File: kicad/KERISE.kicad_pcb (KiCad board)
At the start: 2 copper layers, 42 x 47.5 mm, 116 parts, among them J1 USB_OTG, P1 ANT, P10 Partition, P11 PR_Host, P12 PR_Slave, P13 Partition, P14 Partition, P15 Partition, P16 Partition, P17 COM, P18 Fan, P19 ENC_Host, P2 Motor_L, P20 ENC_Slave, P21 ToF_Host, P22 ToF_Slave, P23 COM, P24 ENC_Host, P25 ENC_Slave, P3 Motor_R, P4 Battery, P5 PR_Host, P6 PR_Slave, P7 Partition, P8 Partition, P9 Partition, Q1 IRFML8244, Q2 IRFML8244, Q3 IRFML8244, Q4 IRFML8244, SW1 SW_Push, SW2 SW_Push, U1 FLASH, U10 MCP73831, U11 FT234XD, U12 AS5048A, U13 ICM-20602, U2 ESP32, U3 XTAL, U4 DRV8835, U5 LXDC2URxx, U6 AD8601, U7 AD8601, U8 AS5048A, U9 VL53L0X

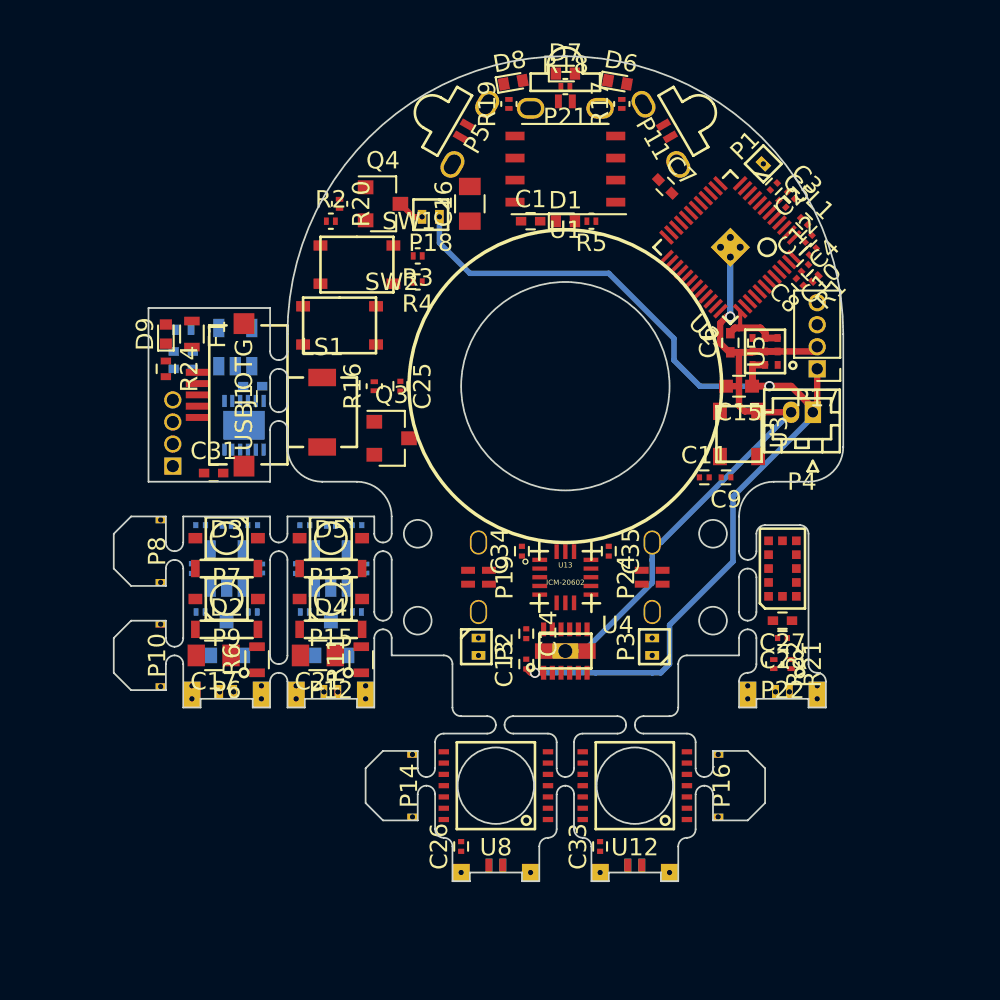
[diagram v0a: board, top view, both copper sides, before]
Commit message: 部品の配置と電源ラインの引き方を変更．
センサ部分にノイズがはいらないように考慮
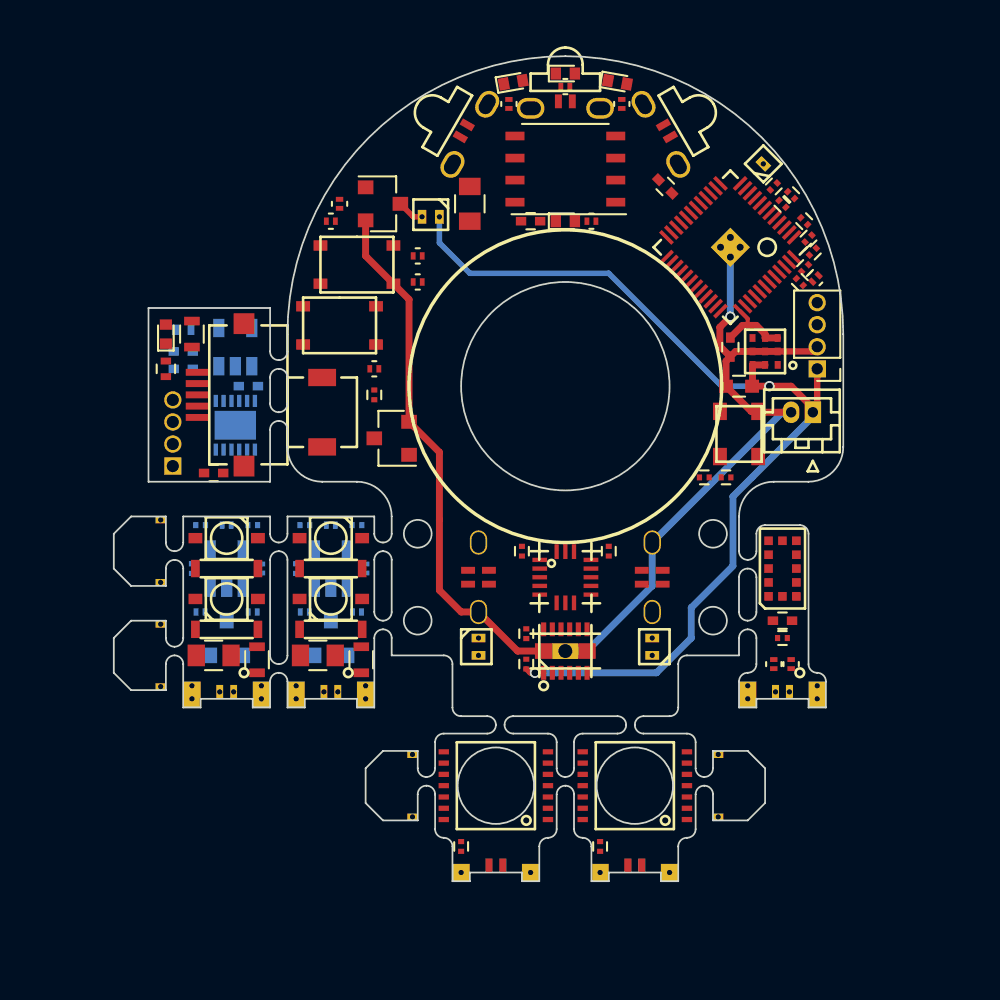
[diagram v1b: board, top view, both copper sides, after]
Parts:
- moved C25 1.58 mm to (137.5, 102.5)
- moved R16 1.00 mm to (137.5, 101.0), turned to 0 degrees
- moved U11 0.50 mm to (129.5, 104.2)
- moved C29 0.25 mm to (130.2, 102.0)
- moved C6 0.25 mm to (158.0, 99.8)
- turned C32 to 0 degrees
- turned Q3 to 180 degrees
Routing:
- net GND: track 38.3 -> 69.7 mm
- net +BATT: track 61.4 -> 59.8 mm
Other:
- net class LED: trace_width 0.3 -> 0.32; via_dia 0.36 -> 0.4; via_drill 0.3 -> 0.36

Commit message: 自動配線成功
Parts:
- C32: moved to F.Cu
- U11: footprint Housings_DFN_QFN:DFN-12-1EP_3x3mm_Pitch0.45mm -> mouse:DFN-12-1EP_3x3mm_Pitch0.45mm
- moved C32 4.60 mm to (126.4, 105.6), turned to 90 degrees
- moved C26 2.50 mm to (142.5, 131.0)
- moved C33 2.50 mm to (150.5, 131.0)
- moved P14 2.50 mm to (140.0, 127.5)
- moved P16 2.50 mm to (157.0, 127.5)
- moved P20 2.50 mm to (144.5, 132.5)
- moved P25 2.50 mm to (152.5, 132.5)
- moved U12 2.50 mm to (152.5, 127.5)
- moved U8 2.50 mm to (144.5, 127.5)
- moved R18 1.25 mm to (147.2, 84.8), turned to 90 degrees
- moved C29 0.79 mm to (129.5, 102.2)
- moved C30 0.71 mm to (126.0, 99.5)
- moved D9 0.71 mm to (125.0, 99.5)
- moved R24 0.71 mm to (125.0, 101.5), turned to 0 degrees
- moved U11 0.62 mm to (128.9, 104.4)
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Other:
- board size 42 x 47.5 mm -> 43 x 50 mm

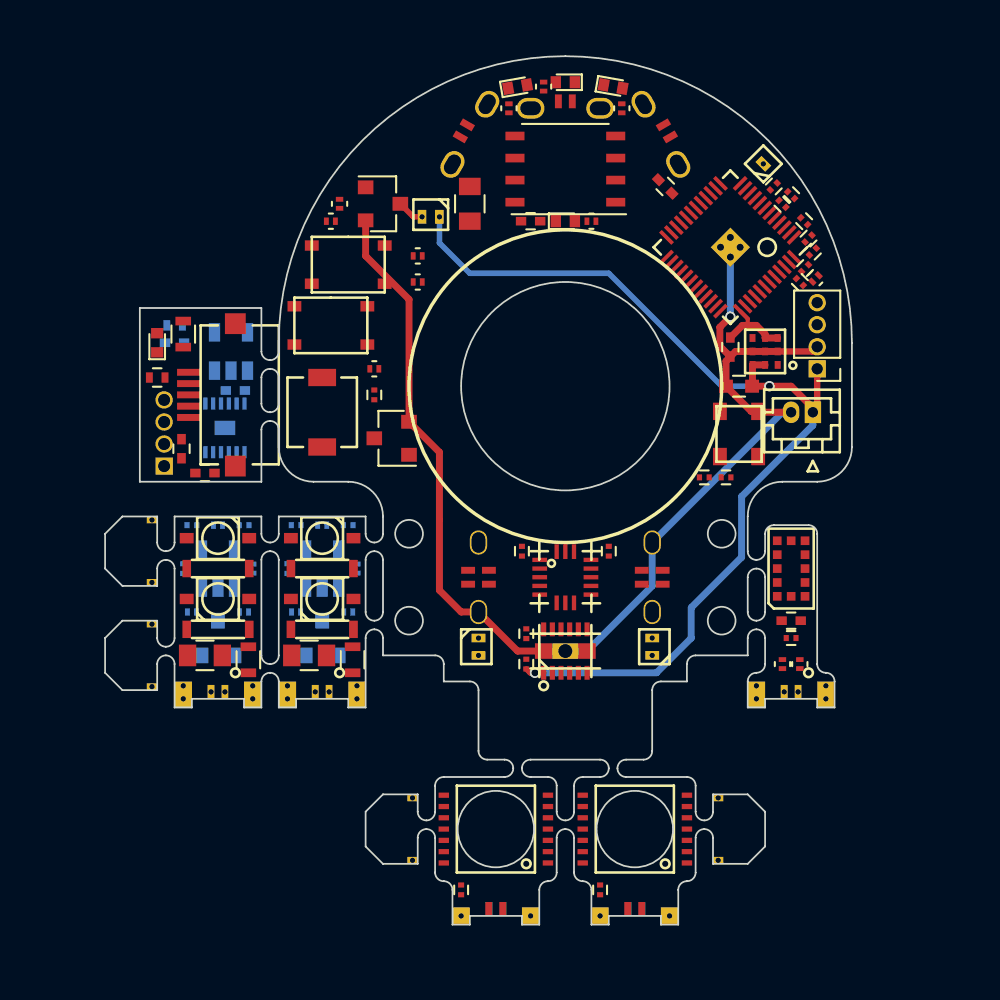
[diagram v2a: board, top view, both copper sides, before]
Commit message: 配線を0.15mmにして自動配線成功
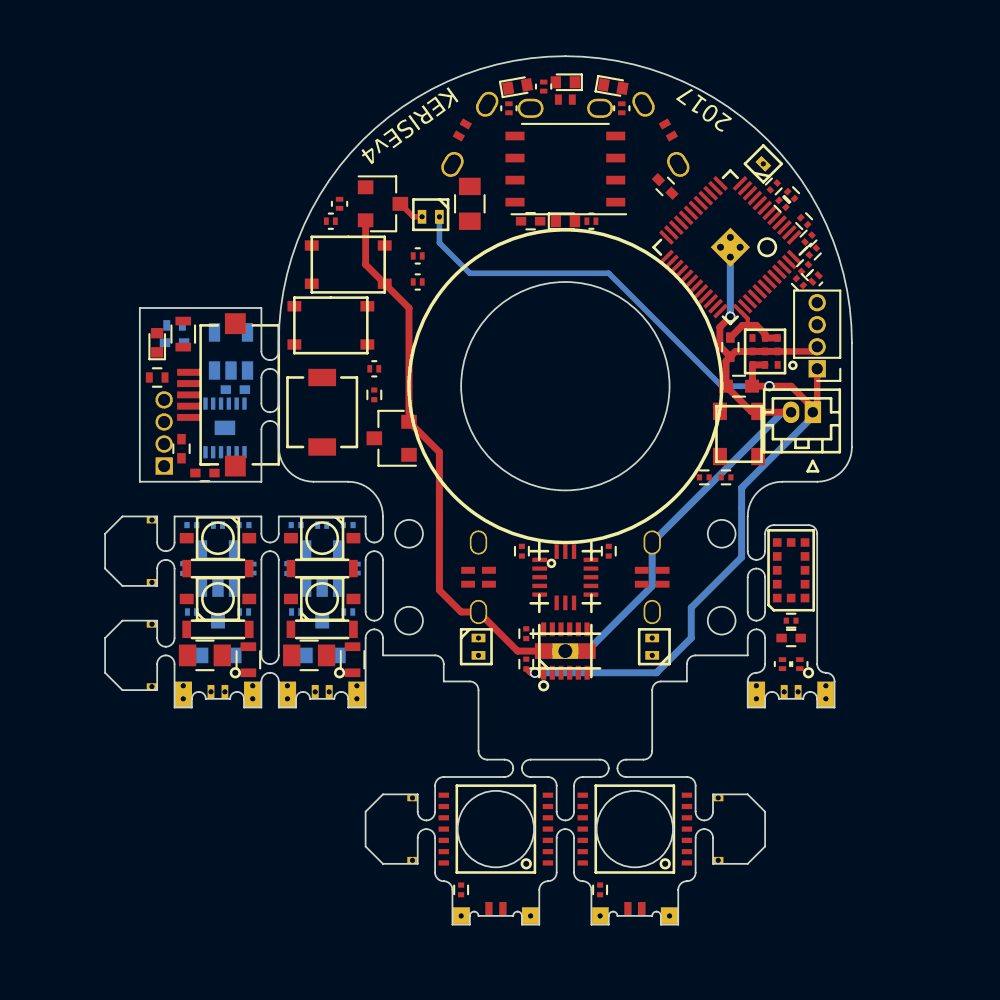
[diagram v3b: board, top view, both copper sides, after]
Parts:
- moved C27 1.00 mm to (161.5, 116.5)
- moved C28 1.00 mm to (161.5, 115.5)
- moved U9 0.10 mm to (161.5, 112.6)
- turned C16 to 270 degrees
- turned C18 to 0 degrees
- turned C22 to 0 degrees
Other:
- outline, holes or cut-outs redrawn
- net class 3.3V: clearance 0.154 -> 0.15; trace_width 0.2 -> 0.16; via_dia 0.34 -> 0.36
- net class BATT: clearance 0.154 -> 0.15; trace_width 0.2 -> 0.15; via_dia 0.34 -> 0.36
- net class Charger: clearance 0.154 -> 0.15; trace_width 0.24 -> 0.2
- net class Default: clearance 0.154 -> 0.15; trace_width 0.154 -> 0.15; via_dia 0.32 -> 0.36
- net class GND: clearance 0.154 -> 0.15; trace_width 0.24 -> 0.16
- net class LED: clearance 0.154 -> 0.15; via_drill 0.36 -> 0.3
- net class Motor: clearance 0.154 -> 0.15; via_drill 0.36 -> 0.3
- rule trace_clearance: 0.154 -> 0.15
- rule trace_min: 0.154 -> 0.15
- rule via_min_size: 0.32 -> 0.3
- board text added: "2017"
- board text added: "KERISEv4"

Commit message: Elecrowに指摘された部分を修正
発注基板
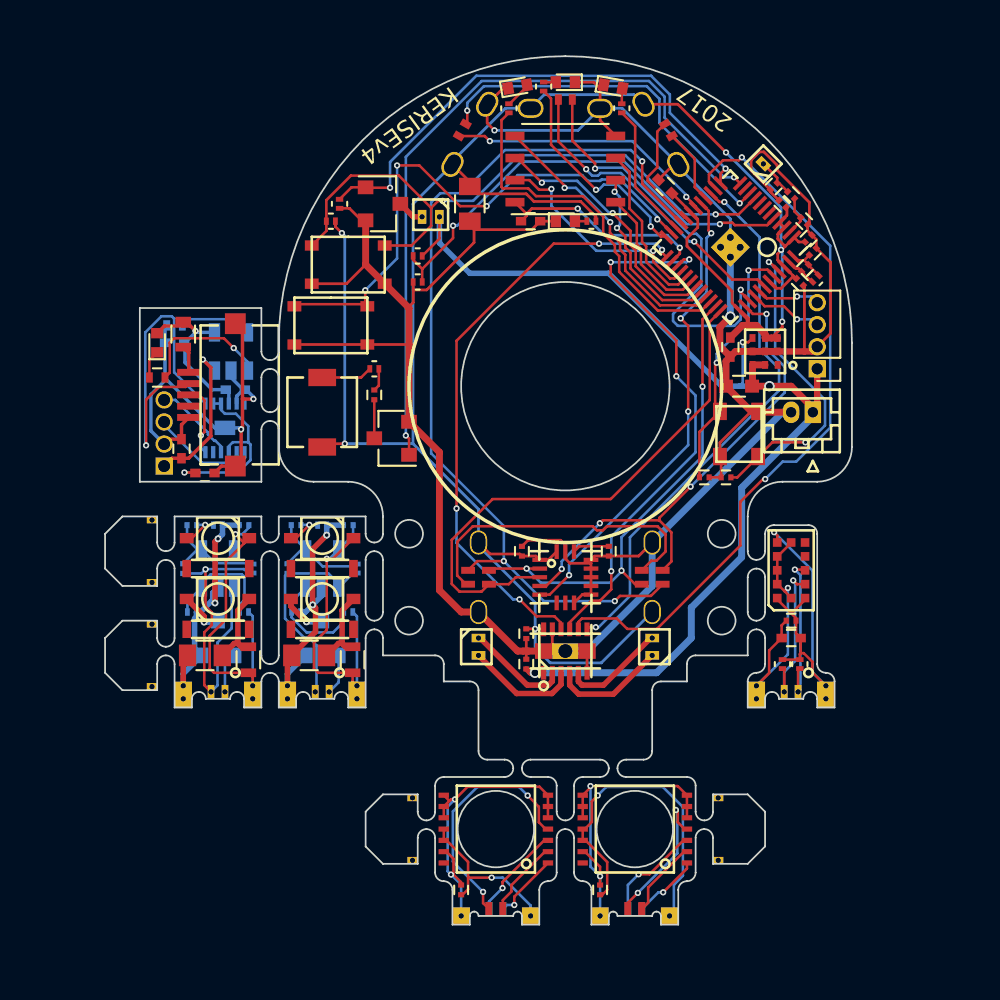
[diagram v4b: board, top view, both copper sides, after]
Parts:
- added G***: LOGO, mouse:KERI_9mm, B.Cu at (148.5, 89.2)
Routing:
- net +3V3: track 4.45 -> 127.7 mm, vias 0 -> 6
- net GND: track 69.7 -> 167.7 mm, vias 1 -> 2
- net SPI-CS-ENC: track 0.00 -> 53.3 mm, vias 0 -> 3
- net MT-IN-R1: track 0.00 -> 42.5 mm, vias 0 -> 2
- net SPEAKER: track 0.00 -> 41.4 mm, vias 0 -> 2
- net Net-(R2-Pad1): track 0.00 -> 36.2 mm, vias 0 -> 2
- net MT-IN-L1: track 0.00 -> 34.8 mm, vias 0 -> 4
- net BUTTON: track 0.00 -> 32.1 mm, vias 0 -> 4
- net MT-IN-L2: track 0.00 -> 32.0 mm, vias 0 -> 4
- net MT-IN-R2: track 0.00 -> 31.9 mm, vias 0 -> 2
- net SPI-MOSI: track 0.00 -> 31.7 mm
- net FAN: track 0.00 -> 29.9 mm, vias 0 -> 2
- net /Writer/USB_GND: track 0.00 -> 29.4 mm, vias 0 -> 2
- net SPI-MISO: track 0.00 -> 28.9 mm, vias 0 -> 4
- net SPI-SCLK: track 0.00 -> 28.0 mm, vias 0 -> 3
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
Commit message: エンコーダの位置を修正，自動配線完了
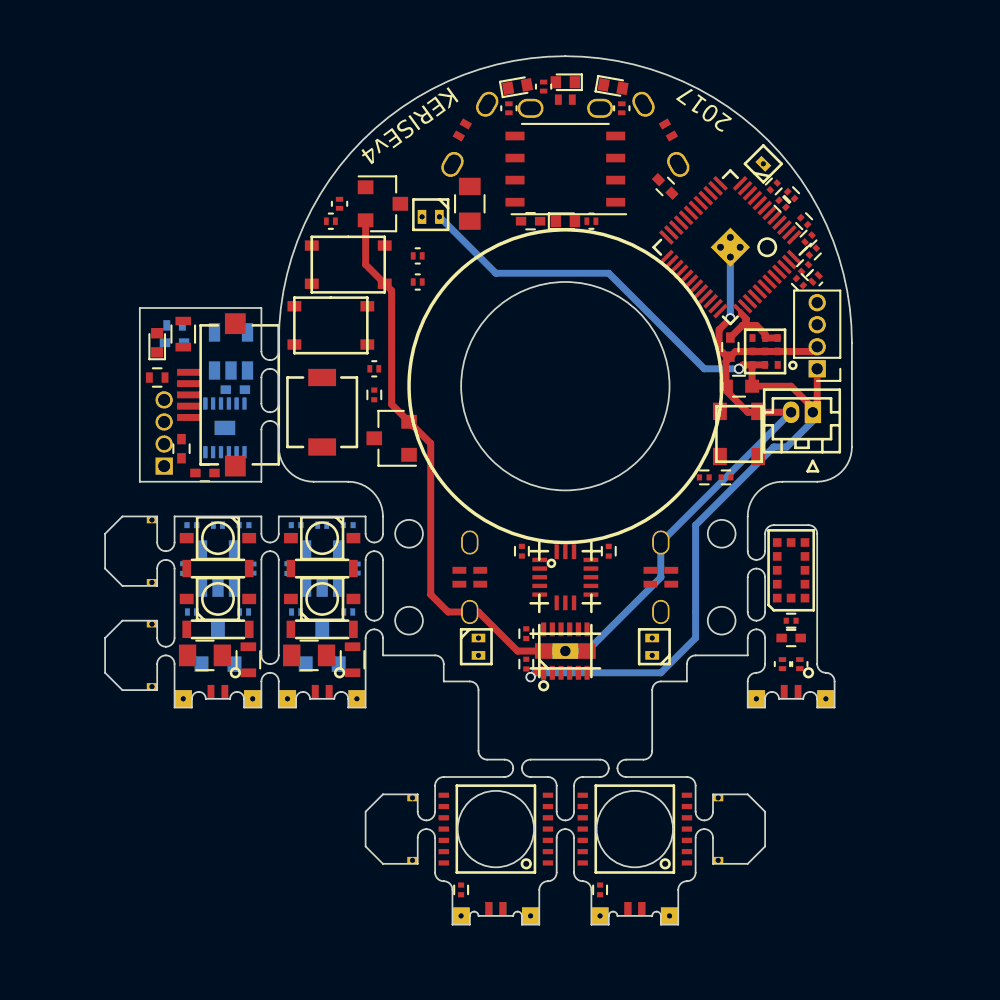
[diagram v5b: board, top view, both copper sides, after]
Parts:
- moved P19 0.50 mm to (143.0, 113.0)
- moved P24 0.50 mm to (154.0, 113.0)
- moved Q1 0.50 mm to (128.5, 117.0)
- moved Q2 0.50 mm to (134.5, 117.0)
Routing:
- net +3V3: track 127.7 -> 5.41 mm, vias 6 -> 0
- net GND: track 167.7 -> 70.0 mm, vias 2 -> 1
- net SPI-CS-ENC: track 53.3 -> 0.00 mm, vias 3 -> 0
- net MT-IN-R1: track 42.5 -> 0.00 mm, vias 2 -> 0
- net SPEAKER: track 41.4 -> 0.00 mm, vias 2 -> 0
- net Net-(R2-Pad1): track 36.2 -> 0.00 mm, vias 2 -> 0
- net MT-IN-L1: track 34.8 -> 0.00 mm, vias 4 -> 0
- net BUTTON: track 32.1 -> 0.00 mm, vias 4 -> 0
- net MT-IN-L2: track 32.0 -> 0.00 mm, vias 4 -> 0
- net MT-IN-R2: track 31.9 -> 0.00 mm, vias 2 -> 0
- net SPI-MOSI: track 31.7 -> 0.00 mm
- net FAN: track 29.9 -> 0.00 mm, vias 2 -> 0
- net /Writer/USB_GND: track 29.4 -> 0.00 mm, vias 2 -> 0
- net SPI-MISO: track 28.9 -> 0.00 mm, vias 4 -> 0
- net SPI-SCLK: track 28.0 -> 0.00 mm, vias 3 -> 0
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
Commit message: 3.3Vの電源ラインを強化，変換基板を付属
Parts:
- added U14: FLASH, Housings_DFN_QFN:DFN-8-1EP_3x2mm_Pitch0.5mm, F.Cu at (120.5, 102.5)
- added U15: FLASH, mouse:SOIJ-8_5.3x5.3mm_Pitch1.27mm_th, F.Cu at (120.5, 102.5)
- U1: footprint mouse:DFN-8-1EP_6x5mm_Pitch1.27mm_SmallFlag -> mouse:SOIJ-8_5.3x5.3mm_Pitch1.27mm
- moved D1 30.5 mm to (148.5, 123.0)
- moved R5 30.5 mm to (150.0, 123.0)
- moved C1 2.46 mm to (144.2, 93.5), turned to 180 degrees
- moved C16 0.56 mm to (143.5, 91.2)
- moved U1 0.50 mm to (148.5, 90.0)
- moved G*** 0.25 mm to (148.5, 89.5)
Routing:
- net +3V3: track 5.41 -> 12.3 mm, vias 0 -> 2
- net Net-(U14-Pad8): track 0.00 -> 2.68 mm
- net Net-(U14-Pad5): track 0.00 -> 2.68 mm
- net Net-(U14-Pad4): track 0.00 -> 2.68 mm
- net Net-(U14-Pad1): track 0.00 -> 2.68 mm
- net Net-(U14-Pad7): track 0.00 -> 2.36 mm
- net Net-(U14-Pad6): track 0.00 -> 2.36 mm
- net Net-(U14-Pad3): track 0.00 -> 2.36 mm
- net Net-(U14-Pad2): track 0.00 -> 2.36 mm
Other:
- board size 43 x 50 mm -> 47 x 50 mm

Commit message: 自動配線を適用
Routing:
- net GND: track 69.9 -> 177.7 mm, vias 1 -> 2
- net +3V3: track 12.3 -> 119.1 mm, vias 2 -> 6
- net Net-(C2-Pad1): track 0.00 -> 53.7 mm
- net SPI-CS-ENC: track 0.00 -> 48.4 mm, vias 0 -> 2
- net SPEAKER: track 0.00 -> 43.2 mm, vias 0 -> 2
- net SPI-CS-AXIS: track 0.00 -> 39.8 mm, vias 0 -> 2
- net MT-IN-R2: track 0.00 -> 36.4 mm, vias 0 -> 2
- net SPI-SCLK: track 0.00 -> 33.7 mm
- net Net-(R2-Pad1): track 0.00 -> 33.1 mm, vias 0 -> 2
- net MT-IN-L1: track 0.00 -> 32.6 mm, vias 0 -> 2
- net MT-IN-R1: track 0.00 -> 31.9 mm, vias 0 -> 2
- net SPI-MISO: track 0.00 -> 30.1 mm, vias 0 -> 3
- net FAN: track 0.00 -> 28.6 mm, vias 0 -> 2
- net /Writer/USB_GND: track 0.00 -> 27.7 mm, vias 0 -> 1
- net BUTTON: track 0.00 -> 26.4 mm, vias 0 -> 2
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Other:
- outline, holes or cut-outs redrawn
